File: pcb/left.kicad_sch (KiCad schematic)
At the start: 76 parts, among them J101 Conn_01x06_MountingPin, SW1 SW_Push, SW10 SW_Push, SW101 SW_SPDT, SW11 SW_Push, SW12 SW_Push, SW13 SW_Push, SW14 SW_Push, SW15 SW_Push, SW16 SW_Push, SW17 SW_Push, SW18 SW_Push, SW19 SW_Push, SW2 SW_Push, SW20 SW_Push, SW21 SW_Push, SW22 SW_Push, SW23 SW_Push, SW24 SW_Push, SW25 SW_Push, SW26 SW_Push, SW27 SW_Push, SW28 SW_Push, SW29 SW_Push, SW3 SW_Push, SW30 SW_Push, SW31 SW_Push, SW32 SW_Push, SW33 SW_Push, SW34 SW_Push, SW35 SW_Push, SW4 SW_Push, SW5 SW_Push, SW6 SW_Push, SW7 SW_Push, SW8 SW_Push, SW9 SW_Push, U101 BLEMicroPro

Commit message: Adapt split keyboard PCBs for AAA battery holders
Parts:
- BT101: footprint Library:battery_holder -> Library:battery_holder_AAA_1x_P55mm
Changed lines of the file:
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@@
 			)
 		)
-		(property "Footprint" "Library:battery_holder"
+		(property "Footprint" "Library:battery_holder_AAA_1x_P55mm"
 			(at 142.24 138.176 90)
 			(effects
@@
 			)
 		)
-		(property "Datasheet" "~"
+		(property "Datasheet" "https://www.monotaro.com/p/6855/7539/"
 			(at 142.24 138.176 90)
 			(effects
@@
 			)
 		)
-		(property "Description" "Single-cell battery"
+		(property "Description" "AAA single-cell holder: GB-BH-4X1-WP"
 			(at 142.24 139.7 0)
 			(effects

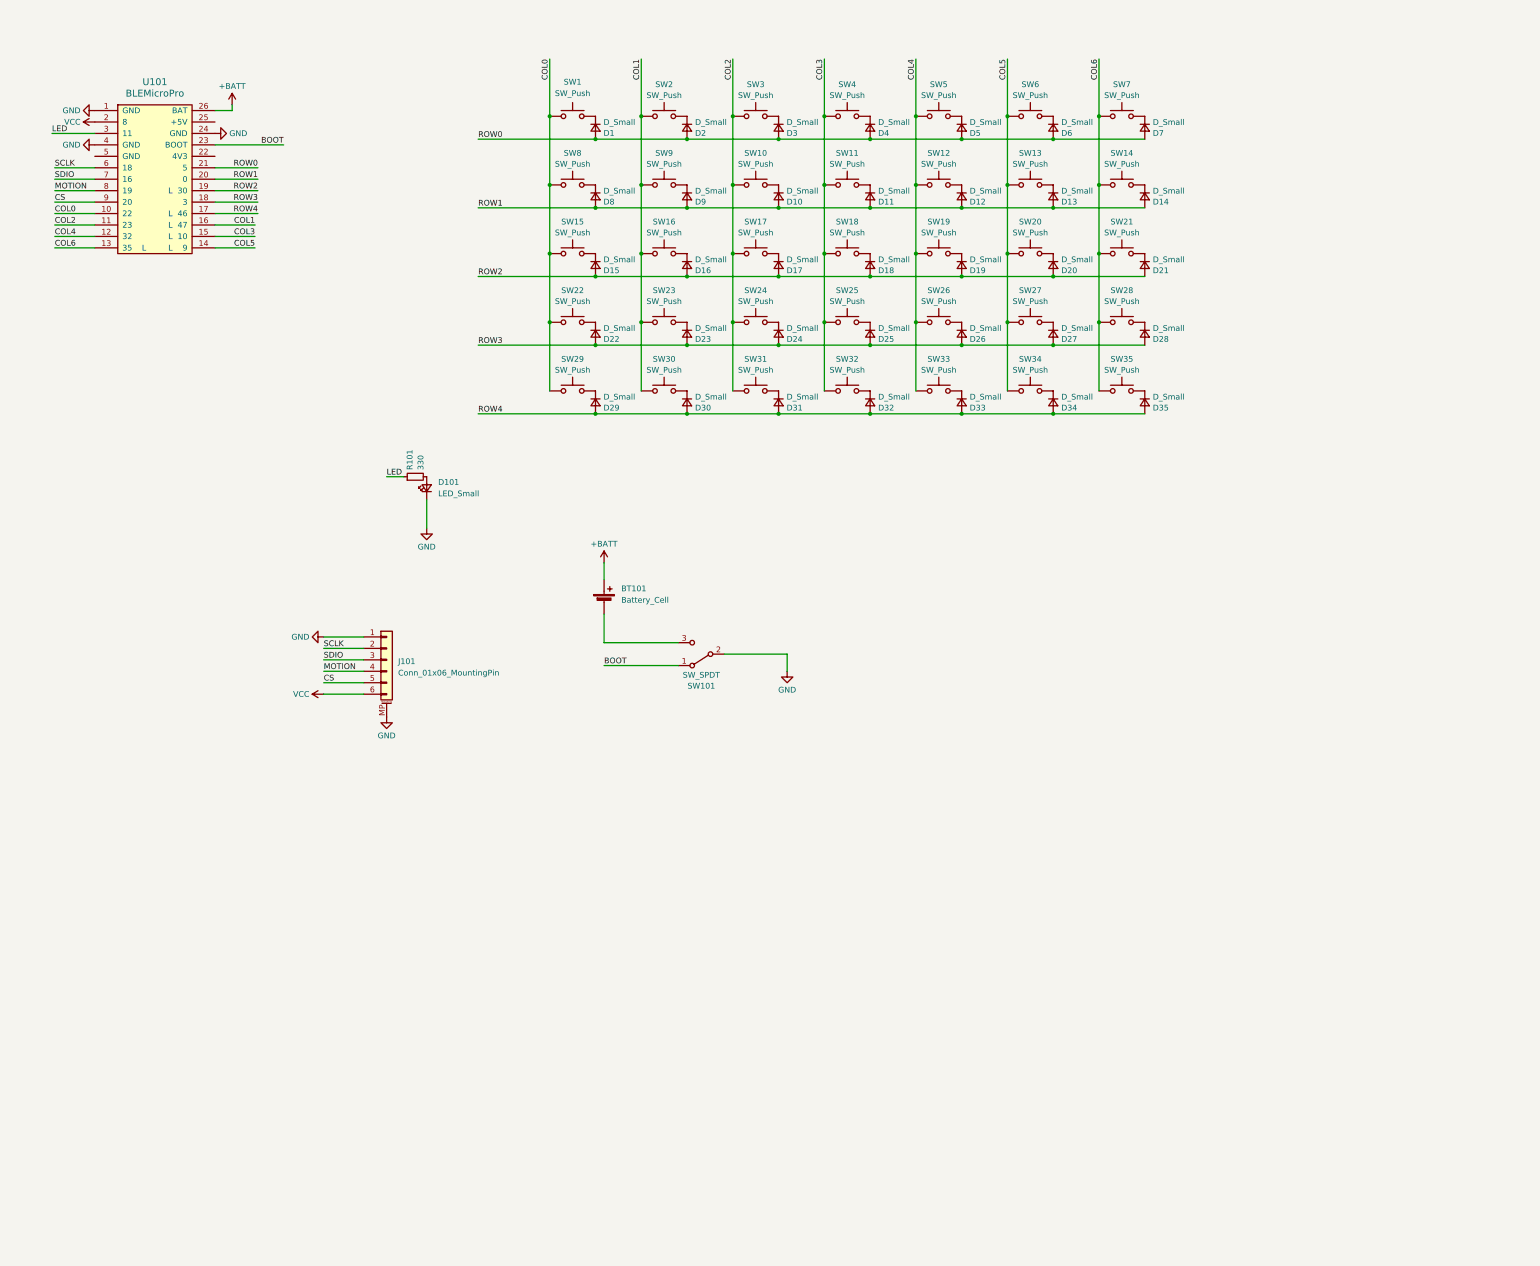
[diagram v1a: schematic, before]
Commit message: Prepare split keyboard PCBs for JLCPCB assembly
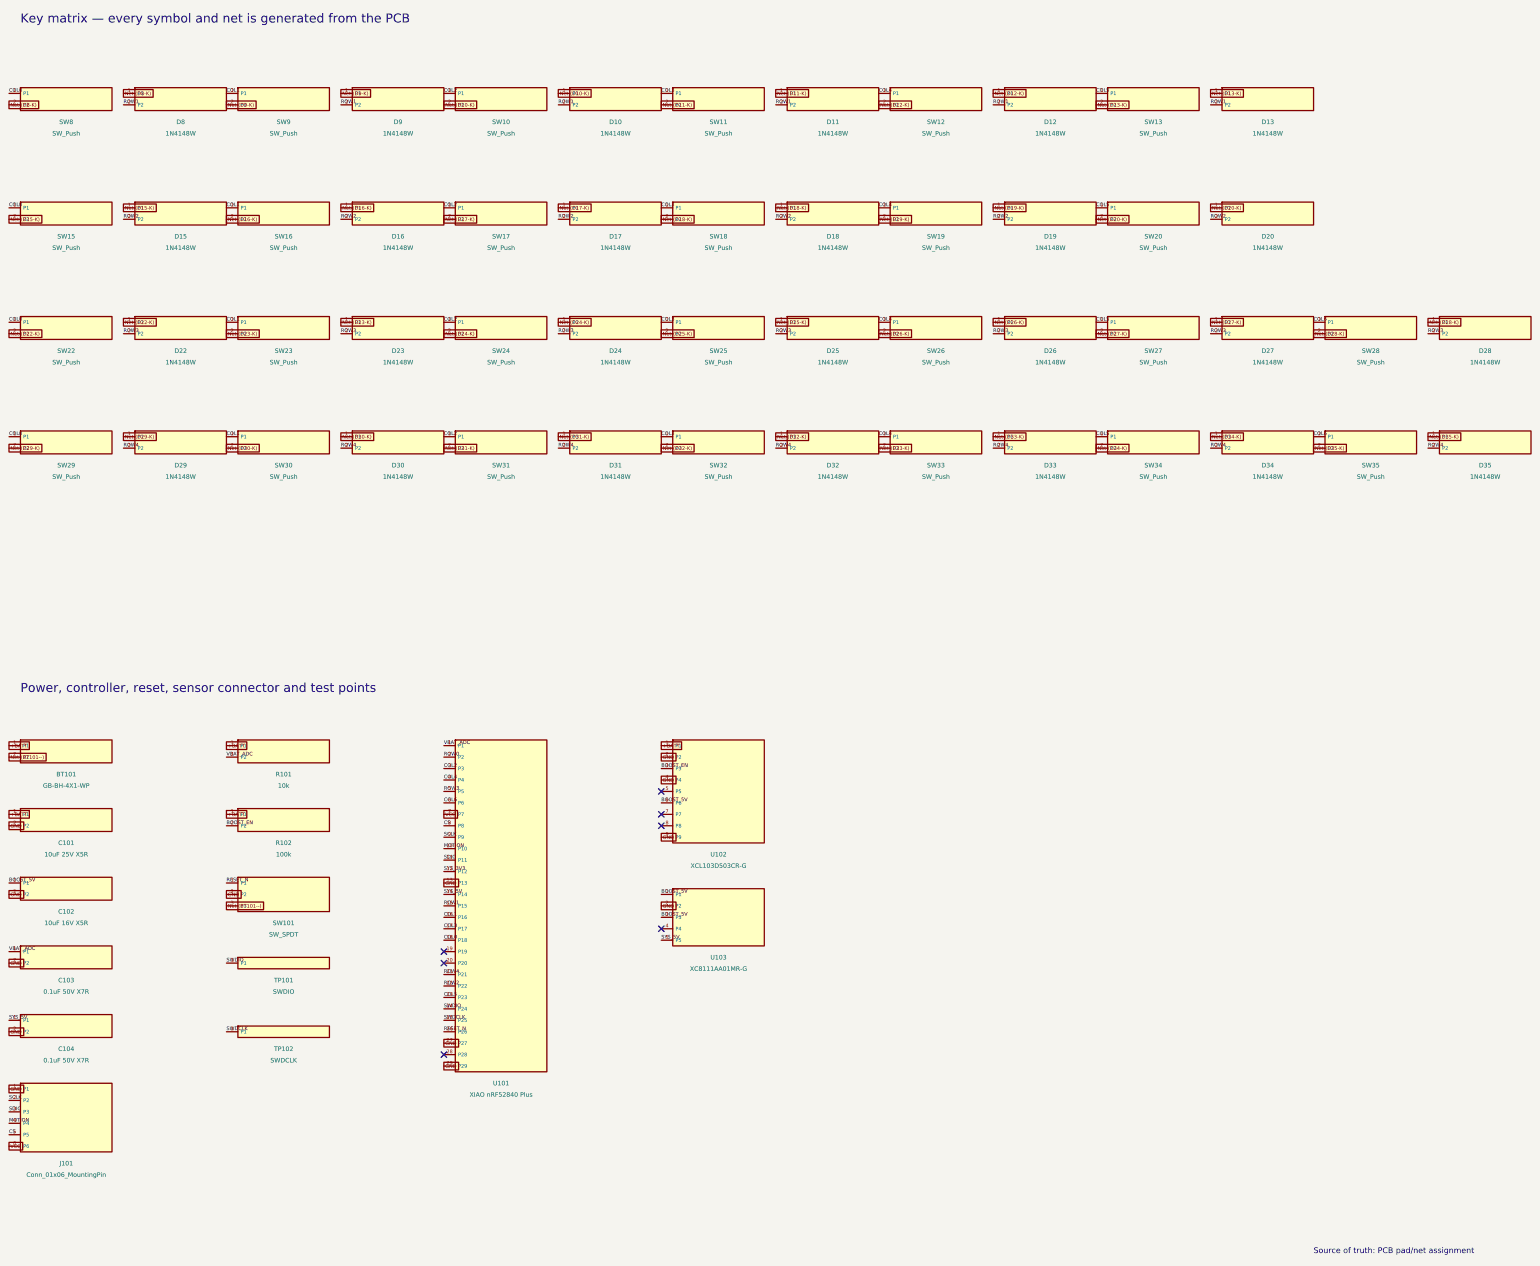
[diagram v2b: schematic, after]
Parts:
- removed BT101: Battery_Cell, Library:battery_holder_AAA_1x_P55mm, symbol Library:Battery_Cell
- removed D1, D10, D11, D12, D13, D14, D15, D16, D17, D18, D19, D2, D20, D21, D22, D23, D24, D25, D26, D27, D28, D29, D3, D30, D31, D32, D33, D34, D35, D4, D5, D6, D7, D8, D9: D_Small, Library:D_SOD-123_HandSoldering, symbol Library:D_Small
- removed D101: LED_Small, Library:LED_D3.0mm, symbol Library:LED_Small
- removed J101: Conn_01x06_MountingPin, Library:ffc-6p-adapter, symbol Library:Conn_01x06_MountingPin
- removed R101: 330, Library:R_Axial_DIN0204_L3.6mm_D1.6mm_P5.08mm_Horizontal, symbol Library:R_Small
- removed SW1, SW10, SW11, SW12, SW13, SW14, SW15, SW16, SW17, SW18, SW19, SW2, SW20, SW21, SW22, SW23, SW24, SW25, SW26, SW27, SW28, SW29, SW3, SW30, SW31, SW32, SW33, SW34, SW35, SW4, SW5, SW6, SW7, SW8, SW9: SW_Push, Library:CHOC_V2_SOCKET_HANDSOLDERING_17mm, symbol Library:SW_Push
- removed SW101: SW_SPDT, Library:ISH-1260-HA-G, symbol Library:SW_SPDT
- removed U101: BLEMicroPro, Library:BLEMicroPro, symbol Library:BLEMicroPro
- added BT101: GB-BH-4X1-WP, Library:battery_holder_AAA_1x_P55mm, symbol Torabo:Block2
- added C101: 10uF 25V X5R, Capacitor_SMD:C_0805_2012Metric, symbol Torabo:Block2
- added C102: 10uF 16V X5R, Capacitor_SMD:C_0603_1608Metric, symbol Torabo:Block2
- added C103, C104: 0.1uF 50V X7R, Capacitor_SMD:C_0603_1608Metric, symbol Torabo:Block2
- added D10, D11, D12, D13, D15, D16, D17, D18, D19, D20, D22, D23, D24, D25, D26, D27, D28, D29, D30, D31, D32, D33, D34, D35, D8, D9: 1N4148W, Library:D_SOD-123_HandSoldering, symbol Torabo:Block2
- added J101: Conn_01x06_MountingPin, Library:ffc-6p-adapter, symbol Torabo:Block6
- added R101: 10k, Resistor_SMD:R_0603_1608Metric, symbol Torabo:Block2
- added R102: 100k, Resistor_SMD:R_0603_1608Metric, symbol Torabo:Block2
- added SW10, SW11, SW12, SW13, SW15, SW16, SW17, SW18, SW19, SW20, SW22, SW23, SW24, SW25, SW26, SW27, SW28, SW29, SW30, SW31, SW32, SW33, SW34, SW35, SW8, SW9: SW_Push, Library:CHOC_V2_SOCKET_HANDSOLDERING_17mm, symbol Torabo:Block2
- added SW101: SW_SPDT, Library:ISH-1260-HA-G, symbol Torabo:Block3
- added TP101: SWDIO, TestPoint:TestPoint_Pad_D1.5mm, symbol Torabo:Block1
- added TP102: SWDCLK, TestPoint:TestPoint_Pad_D1.5mm, symbol Torabo:Block1
- added U101: XIAO nRF52840 Plus, Library:XIAO-nRF52840-Plus-SMD, symbol Torabo:Block29
- added U102: XCL103D503CR-G, Library:CL-2025-02, symbol Torabo:Block9
- added U103: XC8111AA01MR-G, Package_TO_SOT_SMD:SOT-23-5, symbol Torabo:Block5
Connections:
- net +BATT: now also BT101.1 (P1), C101.1 (P1), R101.1 (P1), R102.1 (P1), U102.1 (P1)
- net COL0: now also SW15.1 (P1), SW22.1 (P1), SW29.1 (P1), SW8.1 (P1), U101.18 (P18)
- net COL1: now also SW16.1 (P1), SW23.1 (P1), SW30.1 (P1), SW9.1 (P1), U101.16 (P16)
- net COL2: now also SW10.1 (P1), SW17.1 (P1), SW24.1 (P1), SW31.1 (P1), U101.3 (P3)
- net COL3: now also SW11.1 (P1), SW18.1 (P1), SW25.1 (P1), SW32.1 (P1), U101.17 (P17)
- net COL4: now also SW12.1 (P1), SW19.1 (P1), SW26.1 (P1), SW33.1 (P1), U101.4 (P4)
- net COL5: now also SW13.1 (P1), SW20.1 (P1), SW27.1 (P1), SW34.1 (P1), U101.23 (P23)
- net COL6: now also SW28.1 (P1), SW35.1 (P1), U101.6 (P6)
- net CS: now also J101.5 (P5), U101.8 (P8)
- net GND: now also C101.2 (P2), C102.2 (P2), C103.2 (P2), C104.2 (P2), J101.1 (P1), SW101.2 (P2), U101.13 (P13), U101.27 (P27), U101.29 (P29), U102.2 (P2), U102.4 (P4), U102.9 (P9), U103.2 (P2)
- net MOTION: now also J101.4 (P4), U101.10 (P10)
- net ROW0: now also U101.2 (P2)
- net ROW1: now also D10.2 (P2), D11.2 (P2), D12.2 (P2), D13.2 (P2), D8.2 (P2), D9.2 (P2), U101.15 (P15)
- net ROW2: now also D15.2 (P2), D16.2 (P2), D17.2 (P2), D18.2 (P2), D19.2 (P2), D20.2 (P2), U101.22 (P22)
- net ROW3: now also D22.2 (P2), D23.2 (P2), D24.2 (P2), D25.2 (P2), D26.2 (P2), D27.2 (P2), D28.2 (P2), U101.5 (P5)
- net ROW4: now also D29.2 (P2), D30.2 (P2), D31.2 (P2), D32.2 (P2), D33.2 (P2), D34.2 (P2), D35.2 (P2), U101.21 (P21)
- net SCLK: now also J101.2 (P2), U101.9 (P9)
- net SDIO: now also J101.3 (P3), U101.11 (P11)
- net VCC: now also J101.6 (P6), U101.7 (P7)
- new net BOOST_5V: C102.1 (P1), U102.6 (P6), U103.1 (P1), U103.3 (P3)
- new net BOOST_EN: R102.2 (P2), U102.3 (P3)
- new net Net-(BT101--): BT101.2 (P2), SW101.3 (P3)
- new net Net-(D10-K): D10.1 (P1), SW10.2 (P2)
- new net Net-(D11-K): D11.1 (P1), SW11.2 (P2)
- new net Net-(D12-K): D12.1 (P1), SW12.2 (P2)
- new net Net-(D13-K): D13.1 (P1), SW13.2 (P2)
- new net Net-(D15-K): D15.1 (P1), SW15.2 (P2)
- new net Net-(D16-K): D16.1 (P1), SW16.2 (P2)
- new net Net-(D17-K): D17.1 (P1), SW17.2 (P2)
- new net Net-(D18-K): D18.1 (P1), SW18.2 (P2)
- new net Net-(D19-K): D19.1 (P1), SW19.2 (P2)
- new net Net-(D20-K): D20.1 (P1), SW20.2 (P2)
- new net Net-(D22-K): D22.1 (P1), SW22.2 (P2)
- new net Net-(D23-K): D23.1 (P1), SW23.2 (P2)
- new net Net-(D24-K): D24.1 (P1), SW24.2 (P2)
- new net Net-(D25-K): D25.1 (P1), SW25.2 (P2)
- new net Net-(D26-K): D26.1 (P1), SW26.2 (P2)
- new net Net-(D27-K): D27.1 (P1), SW27.2 (P2)
- new net Net-(D28-K): D28.1 (P1), SW28.2 (P2)
- new net Net-(D29-K): D29.1 (P1), SW29.2 (P2)
- new net Net-(D30-K): D30.1 (P1), SW30.2 (P2)
- new net Net-(D31-K): D31.1 (P1), SW31.2 (P2)
- new net Net-(D32-K): D32.1 (P1), SW32.2 (P2)
- new net Net-(D33-K): D33.1 (P1), SW33.2 (P2)
- new net Net-(D34-K): D34.1 (P1), SW34.2 (P2)
- new net Net-(D35-K): D35.1 (P1), SW35.2 (P2)
- new net Net-(D8-K): D8.1 (P1), SW8.2 (P2)
- new net Net-(D9-K): D9.1 (P1), SW9.2 (P2)
- new net RESET_N: SW101.1 (P1), U101.26 (P26)
- new net SWDCLK: TP102.1 (P1), U101.25 (P25)
- new net SWDIO: TP101.1 (P1), U101.24 (P24)
- new net SYS_3V3: U101.12 (P12)
- new net SYS_5V: C104.1 (P1), U101.14 (P14), U103.5 (P5)
- new net VBAT_ADC: C103.1 (P1), R101.2 (P2), U101.1 (P1)
- no-connect marks 0 -> 7
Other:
- note added: "Key matrix — every symbol and net is generated from the PCB"
- note added: "Power, controller, reset, sensor connector and test points"
- note added: "Source of truth: PCB pad/net assignment"
- note removed: "L"

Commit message: WIP: checkpoint single-XIAO PCB and vertical PHD conversion
Preserve the current single-controller PCB, schematics, documentation, and manufacturing artifacts. Include the vertical PHD placement/routing experiment; its candidate boards still fail DRC and are not production-ready.
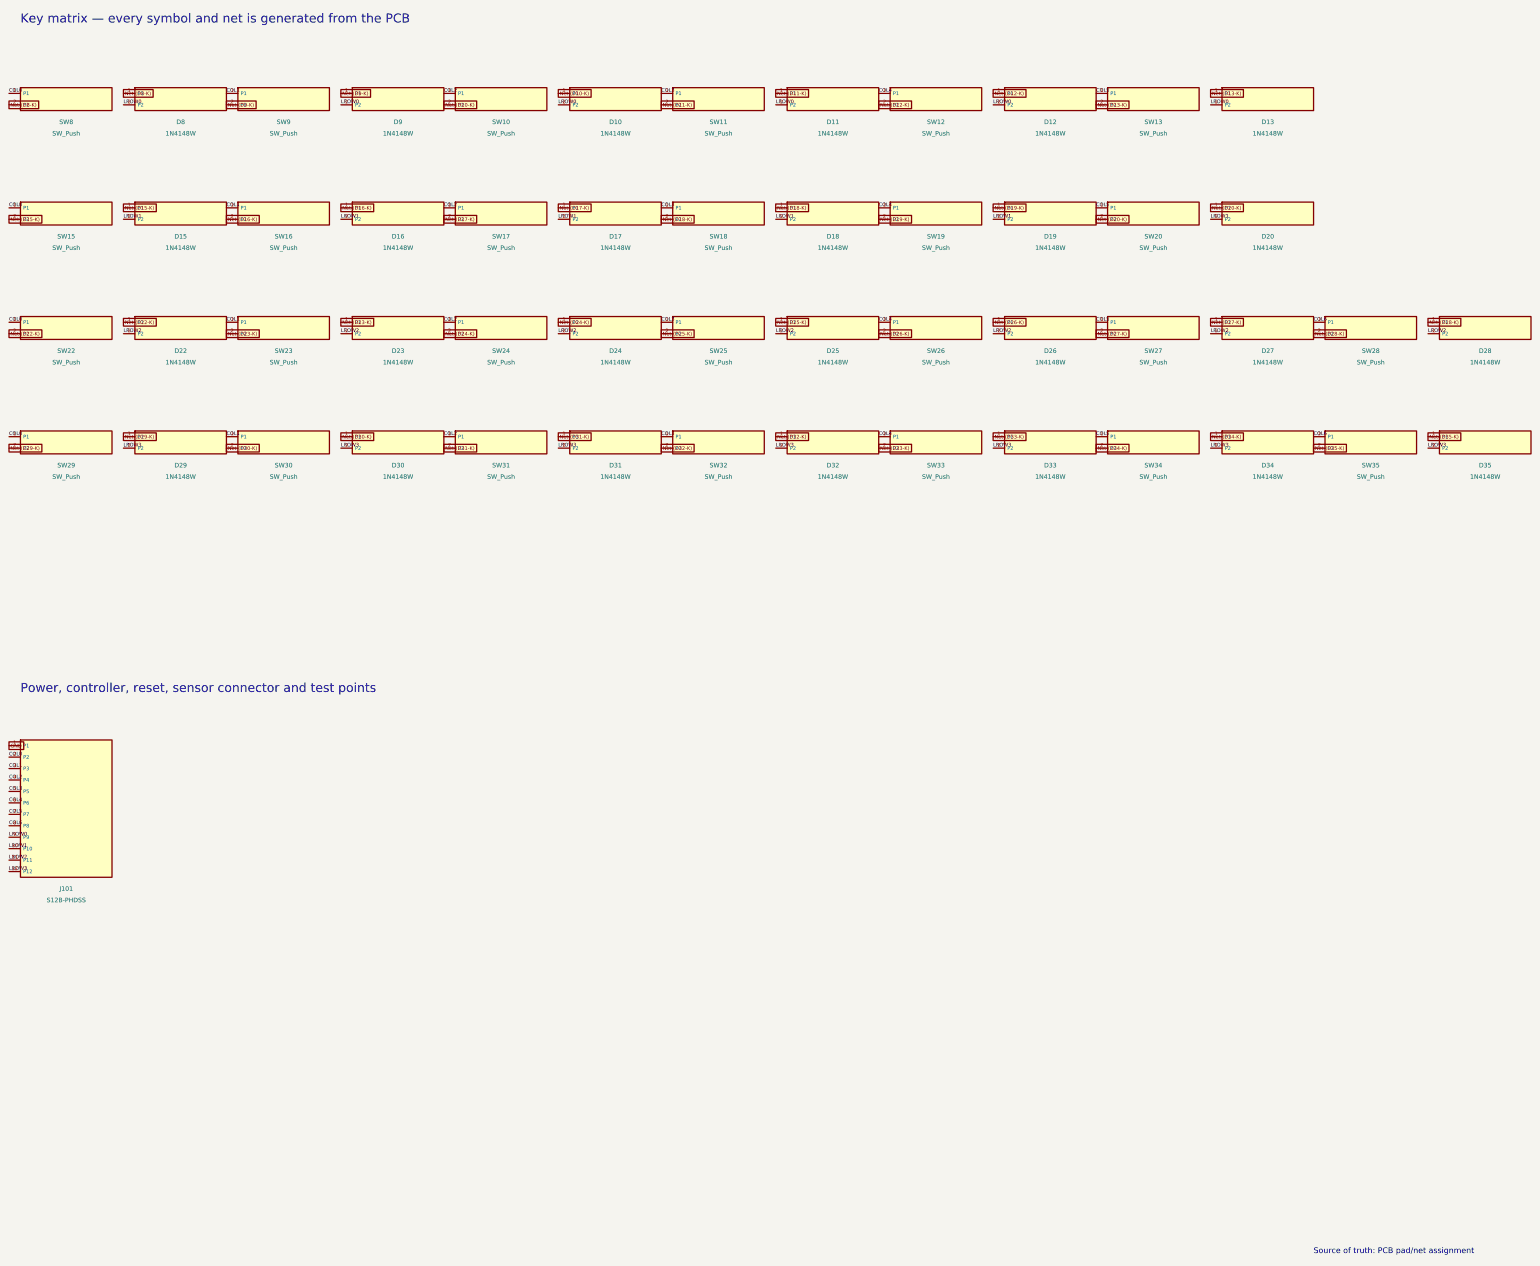
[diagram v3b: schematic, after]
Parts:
- removed BT101: GB-BH-4X1-WP, Library:battery_holder_AAA_1x_P55mm, symbol Torabo:Block2
- removed C101: 10uF 25V X5R, Capacitor_SMD:C_0805_2012Metric, symbol Torabo:Block2
- removed C102: 10uF 16V X5R, Capacitor_SMD:C_0603_1608Metric, symbol Torabo:Block2
- removed C103, C104: 0.1uF 50V X7R, Capacitor_SMD:C_0603_1608Metric, symbol Torabo:Block2
- removed R101: 10k, Resistor_SMD:R_0603_1608Metric, symbol Torabo:Block2
- removed R102: 100k, Resistor_SMD:R_0603_1608Metric, symbol Torabo:Block2
- removed SW101: SW_SPDT, Library:ISH-1260-HA-G, symbol Torabo:Block3
- removed TP101: SWDIO, TestPoint:TestPoint_Pad_D1.5mm, symbol Torabo:Block1
- removed TP102: SWDCLK, TestPoint:TestPoint_Pad_D1.5mm, symbol Torabo:Block1
- removed U101: XIAO nRF52840 Plus, Library:XIAO-nRF52840-Plus-SMD, symbol Torabo:Block29
- removed U102: XCL103D503CR-G, Library:CL-2025-02, symbol Torabo:Block9
- removed U103: XC8111AA01MR-G, Package_TO_SOT_SMD:SOT-23-5, symbol Torabo:Block5
- J101: value Conn_01x06_MountingPin -> S12B-PHDSS; footprint Library:ffc-6p-adapter -> Connector_JST:JST_PHD_S12B-PHDSS_2x06_P2.00mm_Horizontal; symbol Torabo:Block6 -> Torabo:Block12
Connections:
- net CS is gone; now on net COL3: J101.5 (P5)
- net MOTION is gone; now on net COL2: J101.4 (P4)
- net SCLK is gone; now on net COL0: J101.2 (P2)
- net SDIO is gone; now on net COL1: J101.3 (P3)
- net VCC is gone; now on net COL4: J101.6 (P6)
- net COL5: now also J101.7 (P7)
- net COL6: now also J101.8 (P8)
- net ROW1 renamed LROW0
- net LROW0: now also J101.9 (P9)
- net ROW2 renamed LROW1
- net LROW1: now also J101.10 (P10)
- net ROW3 renamed LROW2
- net LROW2: now also J101.11 (P11)
- net ROW4 renamed LROW3
- net LROW3: now also J101.12 (P12)
- no-connect marks 7 -> 0

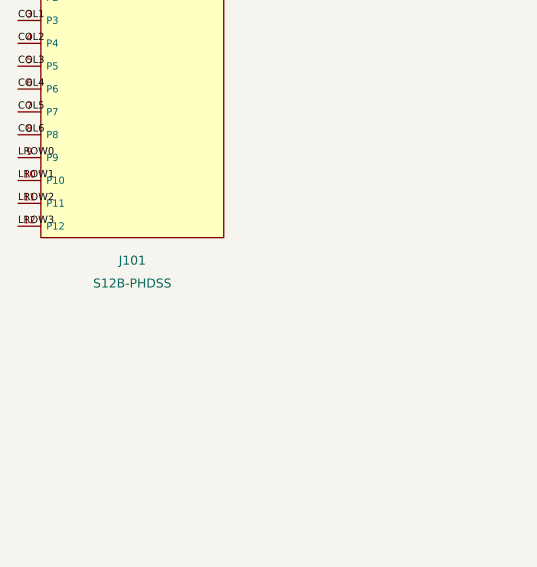
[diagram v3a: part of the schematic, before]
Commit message: Use vertical JST PHD connectors on split PCBs
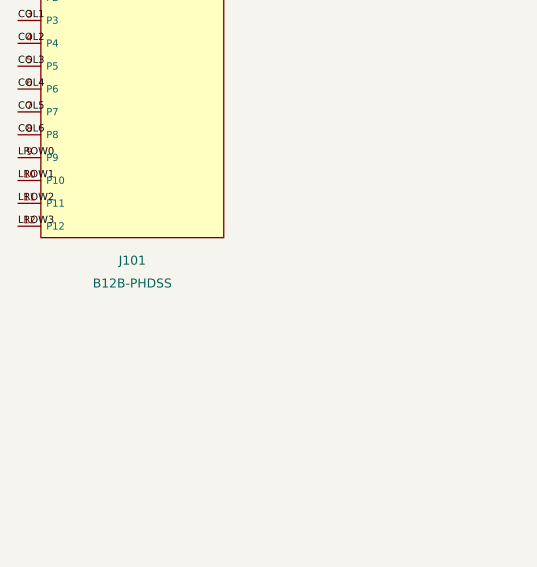
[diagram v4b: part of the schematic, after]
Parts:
- J101: value S12B-PHDSS -> B12B-PHDSS; footprint Connector_JST:JST_PHD_S12B-PHDSS_2x06_P2.00mm_Horizontal -> Connector_JST:JST_PHD_B12B-PHDSS_2x06_P2.00mm_Vertical
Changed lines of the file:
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@@
 			(effects (font (size 1.0 1.0)))
 		)
-		(property "Value" "S12B-PHDSS"
+		(property "Value" "B12B-PHDSS"
 			(at 22.860 205.740 0)
 			(effects (font (size 1.0 1.0)))
 		)
-		(property "Footprint" "Connector_JST:JST_PHD_S12B-PHDSS_2x06_P2.00mm_Horizontal"
+		(property "Footprint" "Connector_JST:JST_PHD_B12B-PHDSS_2x06_P2.00mm_Vertical"
 			(at 22.860 185.420 0)
 			(effects (font (size 1.0 1.0)) (hide yes))
